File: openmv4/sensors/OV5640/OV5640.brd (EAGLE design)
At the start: 35.6 x 16.5 mm, 16 parts, among them U1 OV5640-A71A, U4 ADP150AUJZ-2.8-R7

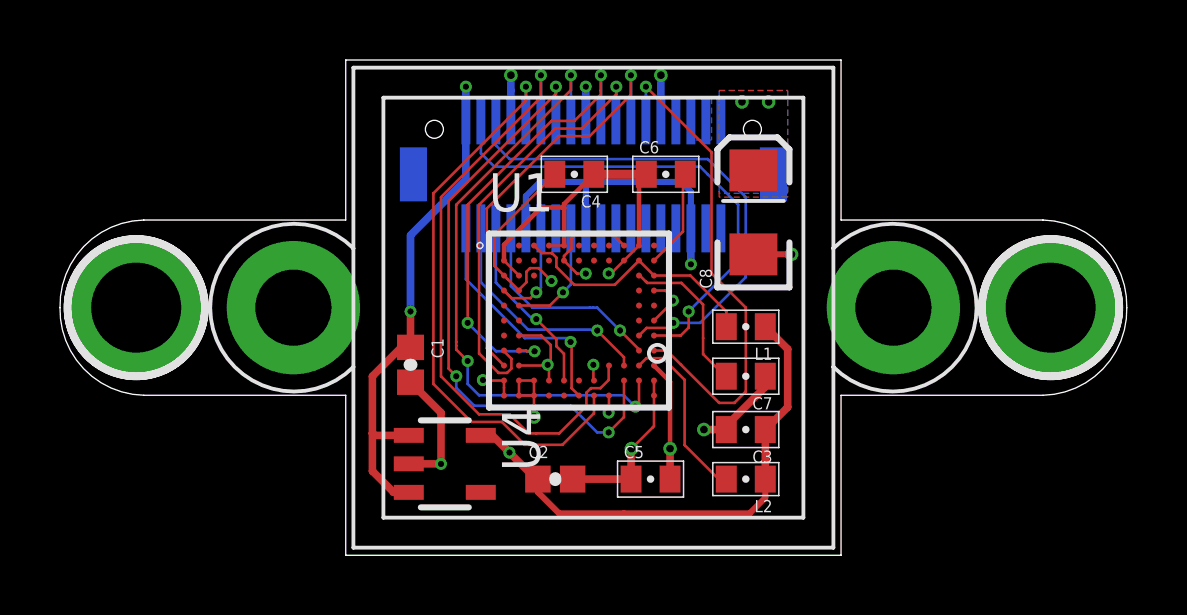
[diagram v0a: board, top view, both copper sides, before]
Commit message: Updated OV5640 circuit
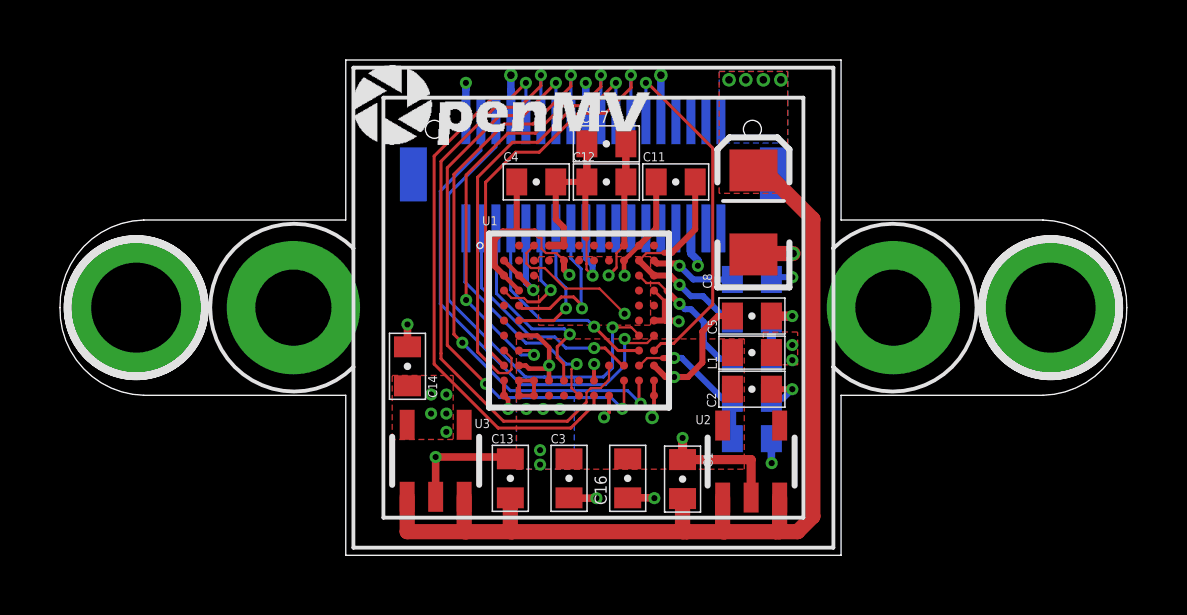
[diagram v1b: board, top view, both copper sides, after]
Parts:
- removed L2: BEAD, heka:0402-CAP
- removed U$1: (no value), openmv:WEEE
- removed U4: ADP150AUJZ-2.8-R7, leptonCustom:SOT23-5
- added C10, C11, C12, C9: 0.1uF, sfe:0402-CAP
- added C13, C14: 1uF, sfe:0402-CAP
- added C15, C16, C17: 10uF, sfe:0402-CAP
- added U$6: (no value), openmv:OMV-LOGO-SMALL
- added U2: ME6211C28M5G, leptonCustom:SOT23-5
- added U3: ME6211C15M5G, leptonCustom:SOT23-5
- C1, C2: value 1 uF -> 1uF; device SparkFun-Capacitors:0402-CAP -> sfe:0402-CAP
- C3: value 0.1uF -> 1uF
- L1: value BEAD -> MPZ1608S181ATAH0
- moved C1 9.84 mm to (11.2, 2.54)
- moved C2 7.21 mm to (13.5, 5.54), turned to 180 degrees
- moved C5 6.40 mm to (13.5, 7.98), turned to 180 degrees
- moved C3 6.11 mm to (7.44, 2.57), turned to 270 degrees
- moved U$2 5.28 mm to (4.24, 0.10)
- moved C6 4.53 mm to (13.5, 9.19), flipped to the bottom
- moved C4 1.30 mm to (6.35, 12.4)
- moved L1 0.89 mm to (13.5, 6.76), turned to 0 degrees
- moved C7 0.62 mm to (13.5, 6.55), flipped to the bottom, turned to 0 degrees
- renumbered U$3 to X1
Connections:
- net N$1 renamed VN
- net N$3 renamed VH
- removed net DVDD: C4.2, C5.2, U1.A9, U1.B5, U1.C1, U1.D2, U1.I11, U1.J1, U1.K1
- removed net PVDD: L2.2, U1.I10
- new net 1V5: C12.2, C14.2, C17.2, C4.2, C5.2, U1.A9, U1.B5, U1.C1, U1.D2, U1.I11, U1.J1, U1.J7, U1.K1, U3.5
- net 2V8: now also C16.2, C2.2, U2.5; no longer C2.1, L2.1, U1.J7, U4.5
- net AVDD: now also C10.2, C11.2, C15.2, C9.2, U1.I10
- net DCMI_FSIN: now also U1.F2
- net GND: now also C1.1, C10.1, C11.1, C12.1, C13.1, C14.1, C15.1, C16.1, C17.1, C2.1, C9.1, U2.2, U3.2; no longer C1.2, C2.2, U4.2
- net VCC: now also C1.2, C13.2, U2.1, U2.3, U3.1, U3.3; no longer C1.1, U4.1, U4.3
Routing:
- net 2V8: track 25.0 -> 2.00 mm, vias 3 -> 5
- net VCC: track 21.2 -> 39.2 mm, vias 7 -> 8
- net 1V5: track 0.00 -> 17.7 mm, vias 0 -> 10
- net DVDD: track 15.7 -> 0.00 mm, vias 4 -> 0
- net AVDD: track 8.68 -> 17.6 mm, vias 0 -> 5
- net PVDD: track 5.96 -> 0.00 mm
- net DCMI_FSIN: track 0.00 -> 4.54 mm, vias 0 -> 1
- net DCMI_CLK: track 16.6 -> 12.2 mm
- net DCMI_RST: track 3.89 -> 5.34 mm
- net I2C1_SCL: track 16.9 -> 15.7 mm
- net DCMI_D0: track 6.09 -> 7.00 mm
- net DCMI_D6: track 20.4 -> 19.6 mm
- net DCMI_VSYNC: track 14.5 -> 15.2 mm
- net DCMI_PWDN: track 3.46 -> 4.07 mm
- net VH: track 5.27 -> 4.66 mm, vias 0 -> 1
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- added copper zone on layer 1, net 1V5
- added copper zone on layer 15, net 1V5
- added copper zone on layer 1, net 2V8
- added copper zone on layer 16, net 2V8
- added copper zone on layer 1, net AVDD
- added copper zone on layer 15, net AVDD
- removed copper zone on layer 15, net DVDD
- removed copper zone on layer 16, net VDDA
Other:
- board text added: "2020/2/09"
- board text added: "OV5640-MOD R3"
- board text removed: "2019/7/5"
- board text removed: "OV5640-MOD R1"
